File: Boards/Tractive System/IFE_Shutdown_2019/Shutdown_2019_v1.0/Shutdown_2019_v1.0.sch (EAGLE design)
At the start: 118 parts, among them Q1 DMN6140L-7, Q10 DMN6140L-7, Q11 DMP3099L-7, Q12 IRLML6346PBF, Q13 IRLML6346PBF, Q14 IRLML6346PBF, Q15 DMP3099L-7, Q16 DMN6140L-7, Q17 IRLML6346PBF, Q18 DMN6140L-7, Q2 DMN6140L-7, Q20 DMN6140L-7, Q21 DMN6140L-7, Q3 DMN6140L-7, Q4 DMN6140L-7, Q5 DMN6140L-7, Q6 DMP3099L-7, Q9 DMN6140L-7, U1 STM32F103CBT6, U2 STM32F103CBT6

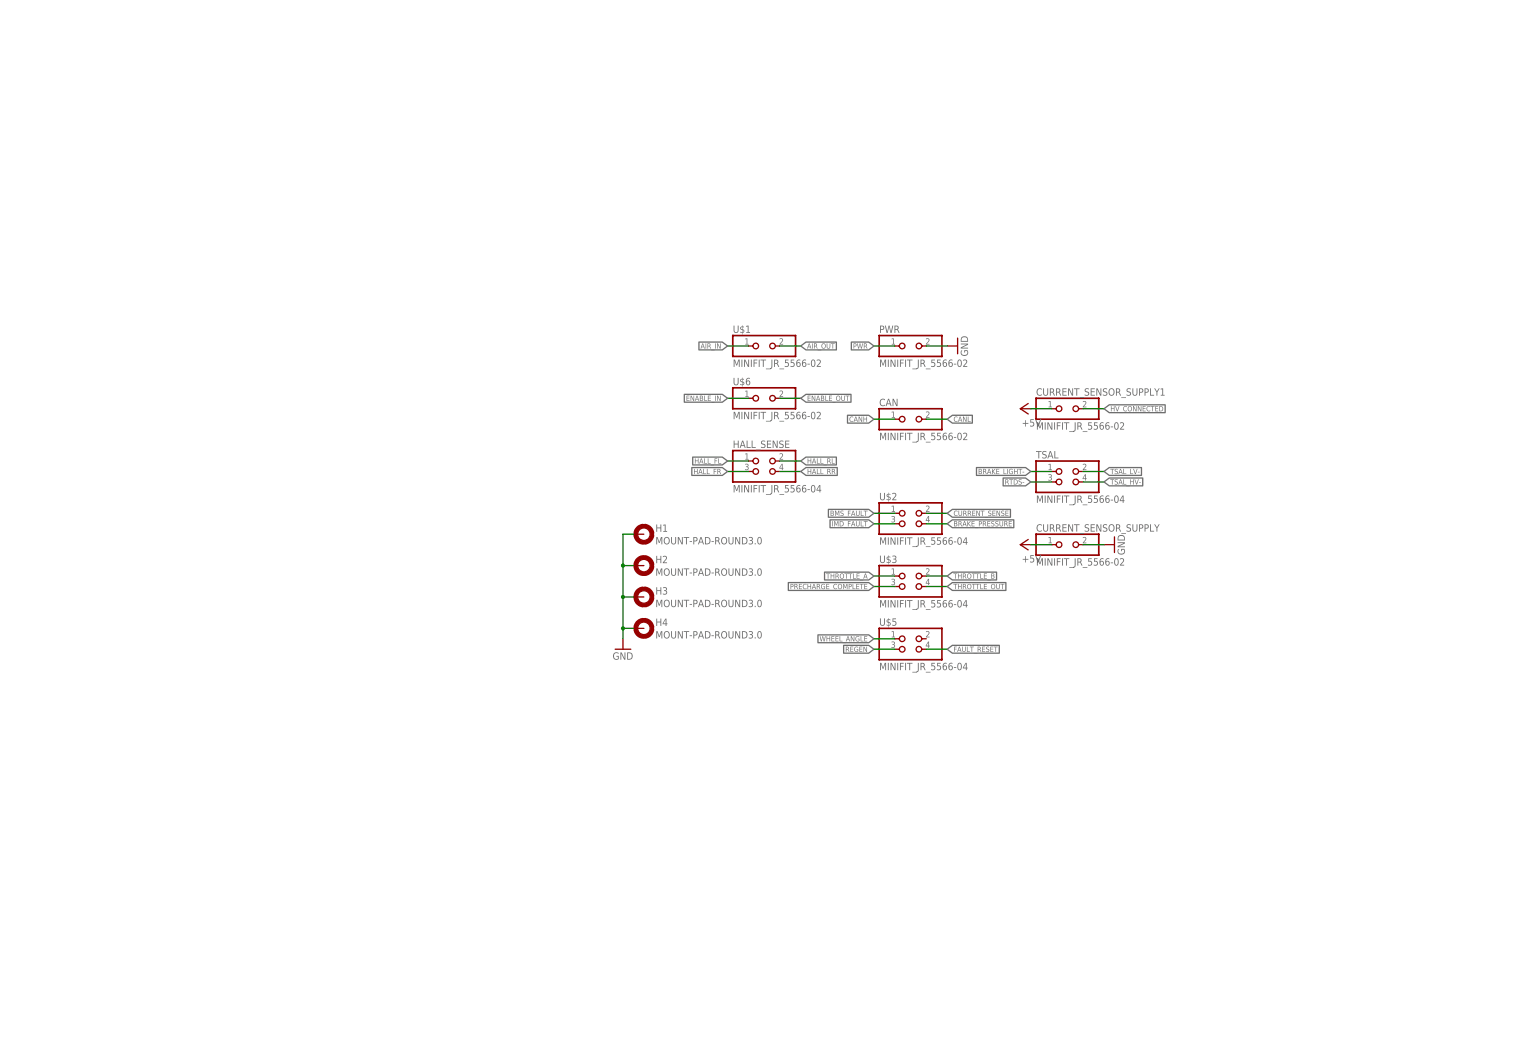
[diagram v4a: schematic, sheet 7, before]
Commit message: More work, inputs protected with zener and LPF
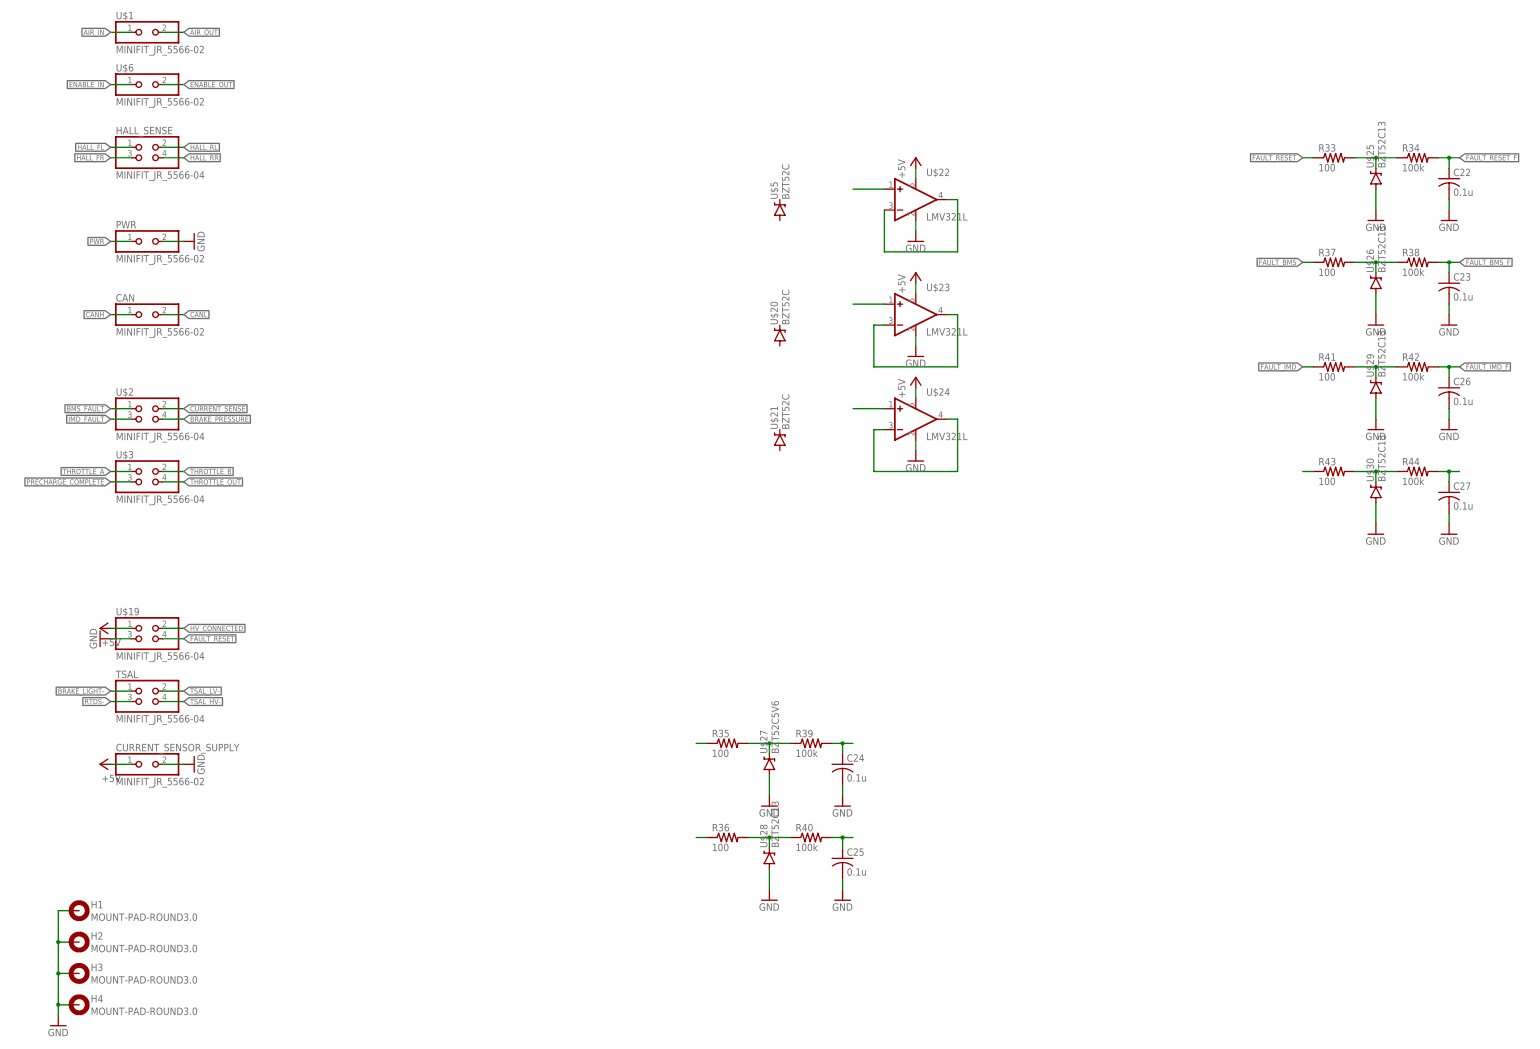
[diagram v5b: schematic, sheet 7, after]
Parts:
- removed CURRENT_SENSOR_SUPPLY1: MINIFIT_JR_5566-02, Display_Custom:MINIFIT_JR_5566-02
- added C22, C23, C24, C25, C26, C27, C28: 0.1u, rcl:C-USC0805
- added R33, R35, R36, R37, R41, R43, R45: 100, rcl:R-US_R0603
- added R34, R38, R39, R40, R42, R44, R46: 100k, rcl:R-US_R0603
- added R47, R48: 10k, rcl:R-US_R0603
- added U$19: MINIFIT_JR_5566-04, Display_Custom:MINIFIT_JR_5566-04
- added U$20, U$21: BZT52C, DIODES_INC:BZT52C
- added U$22, U$23, U$24: LMV321L, STM:LMV321L
- added U$25, U$26, U$28, U$29, U$30, U$31: BZT52C13, DIODES_INC:BZT52C
- added U$27: BZT52C5V6, DIODES_INC:BZT52C
- R25: value 10k -> 1k
- U$5: value MINIFIT_JR_5566-04 -> BZT52C; device Display_Custom:MINIFIT_JR_5566-04 -> DIODES_INC:BZT52C
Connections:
- net N$20 renamed THROTTLE_A_F
- removed net REGEN: U$5.3
- removed net WHEEL_ANGLE: U$5.1
- new net FAULT_BMS_F: C23.1, C6.1, Q3.G, R17.2, R38.2
- new net FAULT_BSPD_F: C7.1, Q5.G, R16.2
- new net FAULT_IMD_F: C26.1, C5.1, Q16.G, R18.2, R42.2
- new net FAULT_RESET_F: C22.1, Q11.G, Q15.G, Q6.G, R25.1, R34.2
- new net N$13: R35.2, R39.1, U$27.C
- new net N$26: C24.1, R39.2
- new net N$29: R33.2, R34.1, U$25.C
- new net N$30: C28.1, R46.2
- new net N$33: R35.1
- new net N$36: R45.1
- new net N$37: R37.2, R38.1, U$26.C
- new net N$39: U$22.+IN
- new net N$40: U$22.-IN, U$22.OUT
- new net N$41: U$24.-IN, U$24.OUT
- new net N$45: U$24.+IN
- new net N$46: U$23.+IN
- new net N$47: U$23.-IN, U$23.OUT
- new net N$49: R41.2, R42.1, U$29.C
- new net N$50: R36.2, R40.1, U$28.C
- new net N$51: C25.1, R40.2
- new net N$54: R36.1
- new net N$55: R43.2, R44.1, U$30.C
- new net N$56: C27.1, R44.2
- new net N$57: R43.1
- net +5V: now also R47.1, R48.1, U$19.1, U$22.VDD, U$23.VDD, U$24.VDD; no longer CURRENT_SENSOR_SUPPLY1.1
- net FAULT_BMS: now also R37.1; no longer C6.1, Q3.G, R17.2
- net FAULT_BSPD: no longer C7.1, Q5.G, R16.2
- net FAULT_IMD: now also R41.1; no longer C5.1, Q16.G, R18.2
- net FAULT_RESET: now also R33.1, U$19.4; no longer Q11.G, Q15.G, Q6.G, R25.1, U$5.4
- net GND: now also C22.2, C23.2, C24.2, C25.2, C26.2, C27.2, C28.2, U$19.3, U$22.GND, U$23.GND, U$24.GND, U$25.A, U$26.A, U$27.A, U$28.A, U$29.A, U$30.A, U$31.A
- net HV_CONNECTED: now also U$19.2; no longer CURRENT_SENSOR_SUPPLY1.2
- net N$22: now also R47.2
- net N$23: now also R48.2
- net N$7: now also R45.2, R46.1, U$31.C; no longer Q4.D
- net RTDS-: now also Q4.D
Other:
- moved on the sheet: CAN, CURRENT_SENSOR_SUPPLY, H1, H2, H3, H4, HALL_SENSE, PWR, Q18, Q20, Q21, R30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

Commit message: Nearly complete... Just BSPD Circuit left
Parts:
- removed C28: 0.1u, rcl:C-USC0805
- removed R46: 100k, rcl:R-US_R0603
- removed U$20, U$21, U$5: BZT52C, DIODES_INC:BZT52C
- removed U$31: BZT52C13, DIODES_INC:BZT52C
- added C29, C30, C31, C32: 0.1u, rcl:C-USC0805
- added C33, C34, C35, C36: 0.001u, rcl:C-USC0805
- added R49, R51, R53, R55: 100, rcl:R-US_R0603
- added R50, R52, R54, R56: 100k, rcl:R-US_R0603
- added R57, R59, R61, R63: 10, rcl:R-US_R0603
- added R58, R60, R62, R64: 10k, rcl:R-US_R0603
- added R65, R66, R67, R68: 1k, rcl:R-US_R0603
- added U$32, U$33, U$34, U$35, U$36, U$37, U$38, U$39: BZT52C5V6, DIODES_INC:BZT52C
- R45: value 100 -> 10k
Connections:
- net N$41 renamed BRAKE_PRESSURE_F
- net N$47 renamed THROTTLE_B_F
- removed net HALL_FL_3_3: U2.PB12
- removed net HALL_FR_3_3: U2.PB13
- removed net HALL_RL_3_3: U2.PB14
- removed net HALL_RR_3_3: U2.PB15
- removed net N$18: U1.PA9
- removed net N$22: R47.2, U$12.SDA
- removed net N$23: R48.2, U$12.SCL
- removed net N$30: C28.1, R46.2
- removed net N$36: R45.1
- removed net N$40: U$22.-IN, U$22.OUT
- removed net N$5: U1.PA8
- removed net N$7: R45.2, R46.1, U$31.C
- removed net REGEN_3_3: U1.PA1
- new net HALL_FL_F: C33.1, R58.2, U2.PB12
- new net HALL_FR_F: C34.1, R60.2, U2.PB13
- new net HALL_RL_F: C35.1, R62.2, U2.PB14
- new net HALL_RR_F: C36.1, R64.2, U2.PB15
- new net N$20: R49.2, R50.1, U$32.C
- new net N$38: C29.1, R50.2
- new net N$52: R51.2, R52.1, U$33.C
- new net N$53: C30.1, R52.2
- new net N$59: R53.2, R54.1, U$34.C
- new net N$60: C31.1, R54.2
- new net N$62: R55.2, R56.1, U$35.C
- new net N$63: C32.1, R56.2
- new net N$64: R55.1
- new net N$65: R57.2, R58.1, R65.1, U$36.C
- new net N$68: R59.2, R60.1, R66.1, U$37.C
- new net N$71: R61.2, R62.1, R67.1, U$38.C
- new net N$74: R63.2, R64.1, R68.1, U$39.C
- net +5V: now also R45.2, R65.2, R66.2, R67.2, R68.2
- net BRAKE_PRESSURE: now also R53.1
- net GND: now also C29.2, C30.2, C31.2, C32.2, C33.2, C34.2, C35.2, C36.2, U$32.A, U$33.A, U$34.A, U$35.A, U$36.A, U$37.A, U$38.A, U$39.A; no longer C28.2, U$31.A
- net HALL_FL: now also R57.1
- net HALL_FR: now also R59.1
- net HALL_RL: now also R61.1
- net HALL_RR: now also R63.1
- net SCL_TC: now also R48.2, U$12.SCL
- net SDA_TC: now also R47.2, U$12.SDA
- net THROTTLE_A: now also R51.1
- net THROTTLE_A_F: now also U$22.-IN, U$22.OUT
- net THROTTLE_B: now also R49.1
- net THROTTLE_OUT: now also R45.1
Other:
- moved on the sheet: C21, Q18, Q20, Q21, R30, R31, R32, R45, R47, R48, R7, U$12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

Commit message: Moving to layout of shutdown
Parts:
- removed U$27, U$35: BZT52C5V6, DIODES_INC:BZT52C
- removed U$28, U$30: BZT52C13, DIODES_INC:BZT52C
- added BRAKE, CURR: PV36, BOURNS:PV36
- added C28: 0.1u, resistor:C-USC0603
- added Q7: DMN6140L-7, TRANS:DMN6140L-7
- added R46, R69, R70, R71, R72, R73, R74: 10k, rcl:R-US_R0603
- added U$20, U$5: TS881, STM:TS881
- added U$21: BZT52C13, DIODES_INC:BZT52C
- C24, C27: device rcl:C-USC0805 -> resistor:C-USC0603
- C25: value 0.1u -> 0.01u; device rcl:C-USC0805 -> resistor:C-USC0603
- C31: value 0.1u -> 0.001u
- R11: value 100k -> 1k
- R35: value 100 -> 1k
- R36: value 100 -> 100k; device rcl:R-US_R0603 -> resistor:R-US_R0603
- R39: value 100k -> 10k; device rcl:R-US_R0603 -> resistor:R-US_R0603
- R40, R44: value 100k -> 1k; device rcl:R-US_R0603 -> resistor:R-US_R0603
- R43: value 100 -> 10k; device rcl:R-US_R0603 -> resistor:R-US_R0603
- R49, R51, R53: value 100 -> 10
- R54: value 100k -> 10k
- U$16, U$17: value PV36 -> TS881; device BOURNS:PV36 -> STM:TS881
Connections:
- removed net BMS_FAULT: U$2.1
- removed net BRAKE_IN: R10.1
- removed net BRAKE_PRESSURE_3_3: U1.PA0-WKUP
- removed net CAN_SBTY: U1.PA10
- removed net CURRENT_IN: R8.1
- removed net FAULT_BMS_STATUS: Q2.G
- removed net FAULT_BSPD_STATUS: Q1.G
- removed net FAULT_IMD_STATUS: Q9.G
- removed net I2C1_SCL: U1.PB6
- removed net I2C1_SDA: U1.PB7
- removed net IMD_FAULT: U$2.3
- removed net N$26: C24.1, R39.2
- removed net N$33: R35.1
- removed net N$39: U$22.+IN
- removed net N$4: C4.1, R1.1
- removed net N$45: U$24.+IN
- removed net N$46: U$23.+IN
- removed net N$50: R36.2, R40.1, U$28.C
- removed net N$51: C25.1, R40.2
- removed net N$54: R36.1
- removed net N$55: R43.2, R44.1, U$30.C
- removed net N$56: C27.1, R44.2
- removed net N$57: R43.1
- removed net N$62: R55.2, R56.1, U$35.C
- removed net N$63: C32.1, R56.2
- removed net N$64: R55.1
- removed net THROTTLE_A_3_3: U1.PB0
- removed net THROTTLE_B_3_3: U1.PB1
- removed net THROTTLE_TH: TTH1.TP, U$17.W
- removed net VDDA: U1.VDDA
- new net BRAKE_PRESSURE_F_3_3: R70.1, R71.2, U1.PA0-WKUP
- new net BSPD_BRAKE_COND: C3.1, Q13.G, R1.1
- new net BSPD_CURR_COND: C4.1, Q12.G, R36.1
- new net BSPD_OC: Q17.G, U$17.OUT
- new net BSPD_SC: Q14.G, U$16.OUT
- new net CURRENT_SENSE_F: C25.1, R44.1, U$16.-IN, U$17.+IN, U$20.+IN
- new net CURR_TH: CURR.W, TTH1.TP, U$20.-IN
- new net N$18: R1.2, U$5.OUT
- new net OC_TH: R11.1, R43.2, U$17.-IN
- new net PRECHARGE_COMPLETE_3_3: Q7.D, R74.1, U1.PB6
- new net PRECHARGE_COMP_F: C32.1, Q7.G, R56.2
- new net SC_TH: R39.1, R40.2, U$16.+IN
- new net THROTTLE_A_F_3_3: R69.1, R73.2, U1.PB0
- new net THROTTLE_B_F_3_3: R46.1, R72.2, U1.PB1
- net +3V3: now also R74.2, U1.VDDA
- net +5V: now also BRAKE.A, C24.1, C27.1, C28.1, CURR.A, R35.2, R39.2, U$16.VDD, U$17.VDD, U$20.VDD, U$5.VDD; no longer R1.2, U$16.A, U$17.A
- net BRAKE_PRESSURE_F: now also R10.1, R70.2, U$5.+IN
- net BRAKE_TH: now also BRAKE.W, U$5.-IN; no longer U$16.W
- net CAN_STBY: now also U1.PA10
- net CURRENT_SENSE: now also R44.2, R8.1
- net FAULT_BMS: now also U$2.1
- net FAULT_BMS_STAT: now also Q2.G
- net FAULT_BSPD_STAT: now also Q1.G
- net FAULT_IMD: now also U$2.3
- net FAULT_IMD_STAT: now also Q9.G
- net GND: now also BRAKE.B, C28.2, CURR.B, Q7.S, R40.1, R43.1, R71.1, R72.1, R73.1, U$16.GND, U$17.GND, U$20.GND, U$21.A, U$5.GND; no longer U$16.B, U$17.B, U$27.A, U$28.A, U$30.A, U$35.A
- net N$13: now also R36.2, U$20.OUT; no longer R35.2, R39.1, U$27.C
- net N$2: now also R55.2, R56.1, U$21.C; no longer C3.1, R11.1
- net N$38: now also U$22.+IN
- net N$53: now also U$23.+IN
- net N$59: now also R35.1
- net N$60: now also U$24.+IN
- net PRECHARGE_COMPLETE: now also R55.1
- net THROTTLE_A_F: now also R69.2
- net THROTTLE_B_F: now also R46.2
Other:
- moved on the sheet: C1, C3, C30, C31, C32, C4, R1, R11, R35, R51, R52, R53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

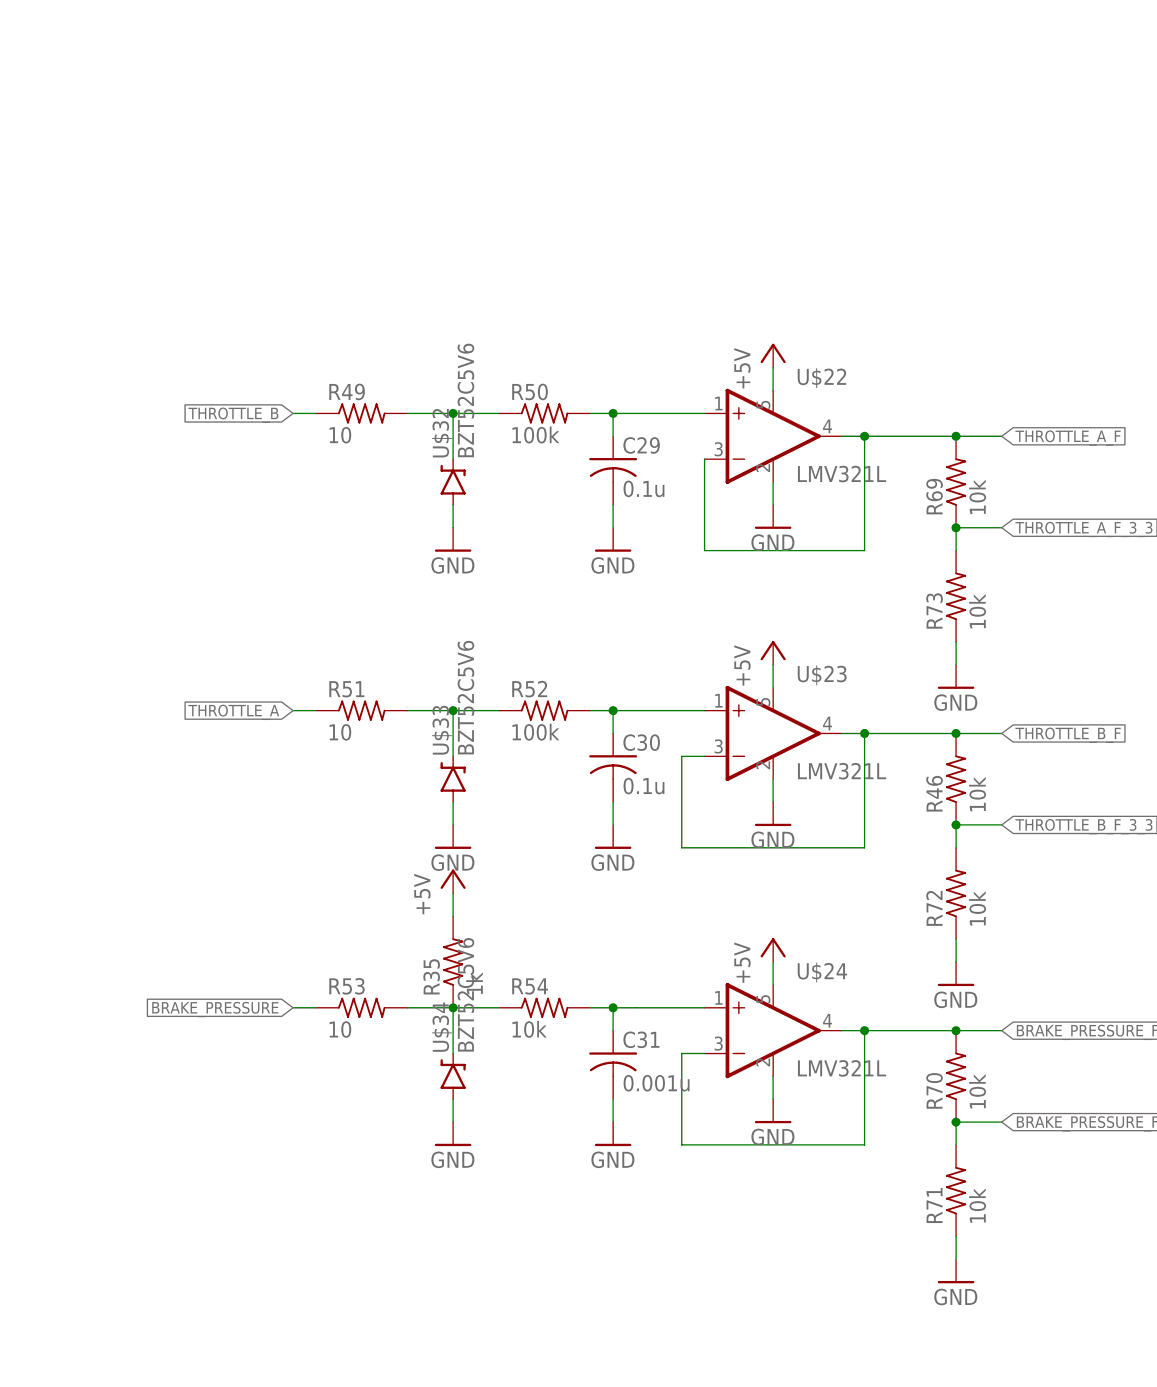
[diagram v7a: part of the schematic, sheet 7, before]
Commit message: Beginning initial Safety route
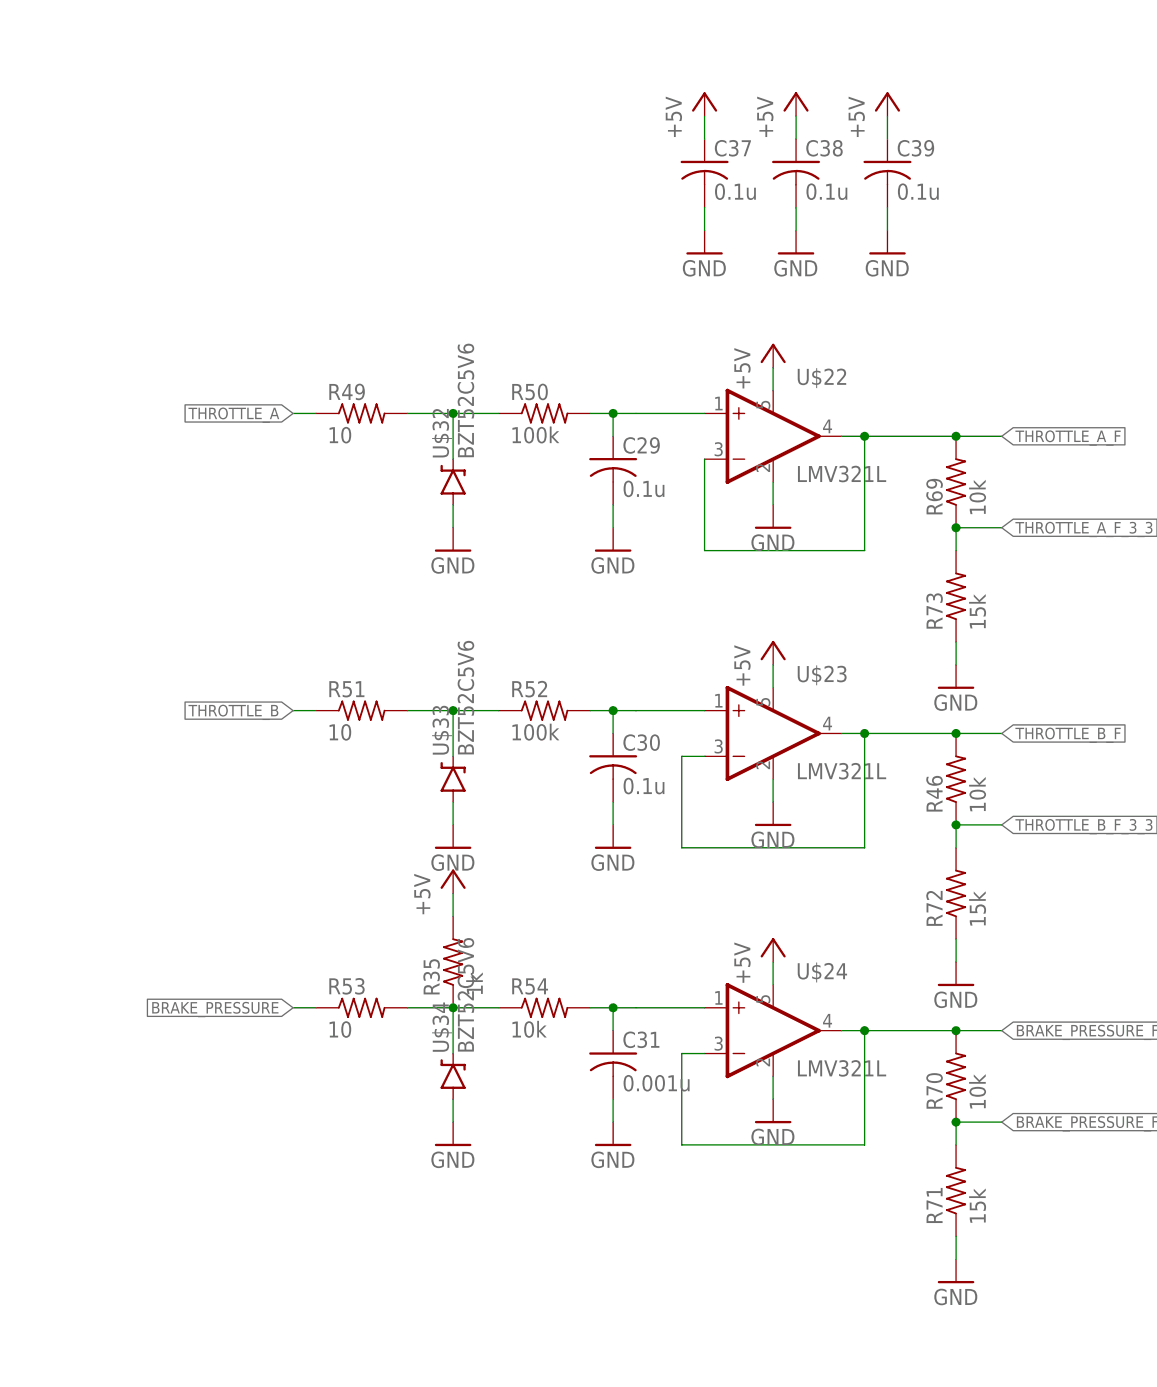
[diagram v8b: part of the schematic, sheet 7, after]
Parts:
- removed R10: 10k, resistor:R-US_R0603
- added C37, C38, C39: 0.1u, resistor:C-USC0603
- R71, R72, R73: value 10k -> 15k
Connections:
- removed net FAULT_BSPD_F: C7.1, Q5.G, R16.2
- net +5V: now also C37.1, C38.1, C39.1; no longer R10.2
- net BRAKE_PRESSURE_F: no longer R10.1
- net FAULT_BSPD: now also C7.1, Q5.G, R16.2
- net GND: now also C37.2, C38.2, C39.2
- net THROTTLE_A: now also R49.1; no longer R51.1
- net THROTTLE_B: now also R51.1; no longer R49.1
